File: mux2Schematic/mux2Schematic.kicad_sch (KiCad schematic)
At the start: 1 part

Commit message: Jackson Schematic Work
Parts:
- added H1, H2, H3, H4: MountingHole, symbol Mechanical:MountingHole
- added J1: Conn_02x12_Odd_Even, symbol Connector_Generic:Conn_02x12_Odd_Even
- added J2: Conn_02x06_Top_Bottom, symbol Connector_Generic:Conn_02x06_Top_Bottom
- added J3, J4: ~, symbol HRL_Custom:Banana_Connector_THT
- added J5, J7: Conn_01x08, symbol Connector_Generic:Conn_01x08
- added J6: ~, symbol HRL_Custom:THT_Wire
- added TP1, TP2, TP3, TP4, TP5, TP6: TestPoint, symbol Connector:TestPoint
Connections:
- net CS_0: now also J2.1 (Pin_1)
- net GND: now also J1.11 (Pin_11), J1.14 (Pin_14), J1.17 (Pin_17), J1.2 (Pin_2), J1.20 (Pin_20), J1.23 (Pin_23), J1.5 (Pin_5), J1.8 (Pin_8), J2.11 (Pin_11), J2.5 (Pin_5); no longer U1.10 (S1), U1.6 (E), U1.7 (V_EE), U1.8 (GND), U1.9 (S2)
- net CS_4: now reaches U1.1 (A4)
- net CS_3: now reaches U1.12 (A3)
- net CS_2: now reaches U1.15 (A2)
- net CS_6: now reaches U1.2 (A6)
- net CS_7: now reaches U1.4 (A7)
- net CS_5: now reaches U1.5 (A5)
- new net: U1.6 (E), U1.7 (V_EE), U1.8 (GND)
- new net CIPO: J2.3 (Pin_3)
- new net COPI: J2.2 (Pin_2)
- new net IOVcc: J2.12 (Pin_12), J2.6 (Pin_6)
- new net OGND: TP3.1, TP5.1
- new net S1: U1.10 (S1)
- new net S2: U1.9 (S2)
- new net SCLK: J2.4 (Pin_4)
- new net Vout_0: J5.1 (Pin_1), TP2.1
- new net Vout_1: J5.2 (Pin_2), TP4.1
- new net supplyGND: J4.
- new net supplyPower: J3.
- new net ~{CLR}: J2.9 (Pin_9)
- new net ~{LDAC}: J2.7 (Pin_7)
- new net ~{RESET}: J2.8 (Pin_8)
- no-connect marks 6 -> 1
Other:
- note added: "8x output SMA blocks"
- note added: "Bot Row"
- note added: "Cap ?"
- note added: "Connectors to VCC on side"
- note added: "LDO 1 to IOVcc supply to 1V8 *Certain*"
- note added: "LDO 2 to VCC supply to 3V3 *Pretty Certain*"
- note added: "October 30, 2024"
- note added: "PCBv1.1 HRL Labs Harvey Mudd Clinic Team"
- note added: "Relevant Testpoints"
- note added: "SMA?"
- note added: "Through Hole or Surface Mount?"
- note added: "Top Row"
- note added: "or"
- moved on the sheet: U1

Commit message: Schematic Draft 1
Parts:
- removed J7: Conn_01x08, symbol Connector_Generic:Conn_01x08
- removed TP1, TP6: TestPoint, symbol Connector:TestPoint
- added C1: 0.1µF, symbol Device:C
- added J10, J11, J12, J13, J14, J7, J9: Conn_02x06_Top_Bottom, symbol Connector_Generic:Conn_02x06_Top_Bottom
- added J15, J16, J17, J18, J19, J20, J21: ~, symbol HRL_Custom:THT_Wire
- added J8: Conn_01x10, symbol Connector_Generic:Conn_01x10
- added JP1: SolderJumper_2_Bridged, symbol Jumper:SolderJumper_2_Bridged
- added JP2: SolderJumper_2_Open, symbol Jumper:SolderJumper_2_Open
- added TP10, TP11, TP12, TP13, TP14, TP15, TP16, TP17, TP18, TP7, TP8, TP9: TestPoint, symbol Connector:TestPoint
- added U2: AMS1117-1.8, Package_TO_SOT_SMD:SOT-223-3_TabPin2, symbol Regulator_Linear:AMS1117-1.8
- added U3: AZ1084-3.3, symbol Regulator_Linear:AZ1084-3.3
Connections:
- net supplyGND is gone; now on net GND: J4.
- net CIPO: now also J10.3 (Pin_3), J11.3 (Pin_3), J12.3 (Pin_3), J13.3 (Pin_3), J14.3 (Pin_3), J7.3 (Pin_3), J9.3 (Pin_3)
- net COPI: now also J10.2 (Pin_2), J11.2 (Pin_2), J12.2 (Pin_2), J13.2 (Pin_2), J14.2 (Pin_2), J7.2 (Pin_2), J8.5 (Pin_5), J9.2 (Pin_2)
- net CS: now also J8.6 (Pin_6)
- net CS_1: now also J7.1 (Pin_1)
- net CS_2: now also J9.1 (Pin_1)
- net CS_3: now also J10.1 (Pin_1)
- net CS_4: now also J11.1 (Pin_1)
- net CS_5: now also J13.1 (Pin_1)
- net CS_6: now also J12.1 (Pin_1)
- net CS_7: now also J14.1 (Pin_1)
- net GND: now also U1.6 (E), U1.7 (V_EE), U1.8 (GND), C1.2, J10.11 (Pin_11), J10.5 (Pin_5), J11.11 (Pin_11), J11.5 (Pin_5), J12.11 (Pin_11), J12.5 (Pin_5), J13.11 (Pin_11), J13.5 (Pin_5), J14.11 (Pin_11), J14.5 (Pin_5), J7.11 (Pin_11), J7.5 (Pin_5), J9.11 (Pin_11), J9.5 (Pin_5), U2.1 (GND), U3.1 (GND)
- net IOVcc: now also J10.12 (Pin_12), J10.6 (Pin_6), J11.12 (Pin_12), J11.6 (Pin_6), J12.12 (Pin_12), J12.6 (Pin_6), J13.12 (Pin_12), J13.6 (Pin_6), J14.12 (Pin_12), J14.6 (Pin_6), J7.12 (Pin_12), J7.6 (Pin_6), J9.12 (Pin_12), J9.6 (Pin_6), U2.2 (VO)
- net OGND: now also TP4.1, TP11.1, TP13.1, TP15.1, TP17.1, TP7.1, TP9.1; no longer TP5.1
- net S0: now also J8.1 (Pin_1)
- net S1: now also J8.2 (Pin_2)
- net S2: now also J8.3 (Pin_3)
- net SCLK: now also J10.4 (Pin_4), J11.4 (Pin_4), J12.4 (Pin_4), J13.4 (Pin_4), J14.4 (Pin_4), J7.4 (Pin_4), J8.4 (Pin_4), J9.4 (Pin_4)
- net VCC: now also J6., J15., J16., J17., J18., J19., J20., J21., JP1.2 (B), U3.2 (VO)
- net Vout_1: now also TP5.1; no longer TP4.1
- net muxPower: now also U1.16 (VCC), C1.1, JP1.1 (A), JP2.2 (B)
- net supplyPower: now also JP2.1 (A), U2.3 (VI), U3.3 (VI)
- net ~{CLR}: now also J10.9 (Pin_9), J11.9 (Pin_9), J12.9 (Pin_9), J13.9 (Pin_9), J14.9 (Pin_9), J7.9 (Pin_9), J8.9 (Pin_9), J9.9 (Pin_9)
- net ~{LDAC}: now also J10.7 (Pin_7), J11.7 (Pin_7), J12.7 (Pin_7), J13.7 (Pin_7), J14.7 (Pin_7), J7.7 (Pin_7), J8.7 (Pin_7), J9.7 (Pin_7)
- net ~{RESET}: now also J10.8 (Pin_8), J11.8 (Pin_8), J12.8 (Pin_8), J13.8 (Pin_8), J14.8 (Pin_8), J7.8 (Pin_8), J8.8 (Pin_8), J9.8 (Pin_8)
- net Vout_2: now reaches J5.3 (Pin_3)
- net Vout_2: now also TP8.1
- net Vout_3: now reaches J5.4 (Pin_4)
- net Vout_3: now also TP10.1
- net Vout_4: now reaches J5.5 (Pin_5)
- net Vout_4: now also TP12.1
- net Vout_5: now reaches J5.6 (Pin_6)
- net Vout_5: now also TP14.1
- net Vout_6: now reaches J5.7 (Pin_7)
- net Vout_6: now also TP16.1
- net Vout_7: now reaches J5.8 (Pin_8)
- net Vout_7: now also TP18.1
- no-connect marks 1 -> 9
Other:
- note added: "8x DAC output blocks"
- note added: "Additional Testpoints"
- note added: "Mux Power and Logic"
- note added: "Power"
- note added: "VCC Ports for Side"
- note added: "Xilinx Digital Input"
- note removed: "8x output SMA blocks"
- note removed: "Cap ?"
- note removed: "Connectors to VCC on side"
- note removed: "LDO 1 to IOVcc supply to 1V8 *Certain*"
- note removed: "LDO 2 to VCC supply to 3V3 *Pretty Certain*"
- note removed: "Relevant Testpoints"
- note removed: "Through Hole or Surface Mount?"
- note removed: "or"
- moved on the sheet: H1, H2, H3, H4, J1, J2, J3, J4, J5, J6, TP2, TP3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

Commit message: Final Draft Schematic
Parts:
- removed J5: Conn_01x08, symbol Connector_Generic:Conn_01x08
- added C2, C4: 10uF, symbol Device:C_Polarized
- added C3, C5: 22uF, symbol Device:C_Polarized
- added J22, J23, J24, J25, J26, J27, J28, J29: ~, symbol HRL_Custom:SMA_Connector
- added J30, J31, J5: Conn_01x10, symbol Connector_Generic:Conn_01x10
- added R1, R2, R3, R4, R5, R6, R7, R8: 10k, symbol Device:R
- C1: value 0.1µF -> 0.1uF
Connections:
- net CS_0: now also J30.1 (Pin_1), R1.1
- net CS_1: now also J30.2 (Pin_2), R2.1
- net CS_2: now also J30.3 (Pin_3), R3.1
- net CS_3: now also J30.4 (Pin_4), R4.1
- net CS_4: now also J30.5 (Pin_5), R5.1
- net CS_5: now also J30.6 (Pin_6), R6.1
- net CS_6: now also J30.7 (Pin_7), R7.1
- net CS_7: now also J30.8 (Pin_8), R8.1
- net GND: now also J8.10 (Pin_10), C2.2, C3.2, C4.2, C5.2, J30.10 (Pin_10), J30.9 (Pin_9)
- net IOVcc: now also C5.1, R1.2, R2.2, R3.2, R4.2, R5.2, R6.2, R7.2, R8.2
- net VCC: now also C3.1
- net Vout_0: now also J22.Center, J31.1 (Pin_1)
- net Vout_1: now also J23.Center, J31.2 (Pin_2)
- net Vout_2: now also J24.Center, J31.3 (Pin_3)
- net Vout_3: now also J25.Center, J31.4 (Pin_4)
- net Vout_4: now also J26.Center, J31.5 (Pin_5)
- net Vout_5: now also J27.Center, J31.6 (Pin_6)
- net Vout_6: now also J28.Center, J31.7 (Pin_7)
- net Vout_7: now also J29.Center, J31.8 (Pin_8)
- net supplyPower: now also C2.1, C4.1
- removed net OGND: TP11.1, TP13.1, TP15.1, TP17.1, TP3.1, TP4.1, TP7.1, TP9.1
- new net OGND_0: J22.Shield, J5.1 (Pin_1), TP3.1
- new net OGND_1: J23.Shield, J5.2 (Pin_2), TP4.1
- new net OGND_2: J24.Shield, J5.3 (Pin_3), TP7.1
- new net OGND_3: J25.Shield, J5.4 (Pin_4), TP9.1
- new net OGND_4: J26.Shield, J5.5 (Pin_5), TP11.1
- new net OGND_5: J27.Shield, J5.6 (Pin_6), TP13.1
- new net OGND_6: J28.Shield, J5.7 (Pin_7), TP15.1
- new net OGND_7: J29.Shield, J5.8 (Pin_8), TP17.1
- no-connect marks 9 -> 12
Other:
- note added: "CS_x Pull Up Resistors"
- note removed: "SMA?"
- moved on the sheet: C1, J15, J16, J17, J18, J19, J20, J21, J6, JP1, JP2, TP11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

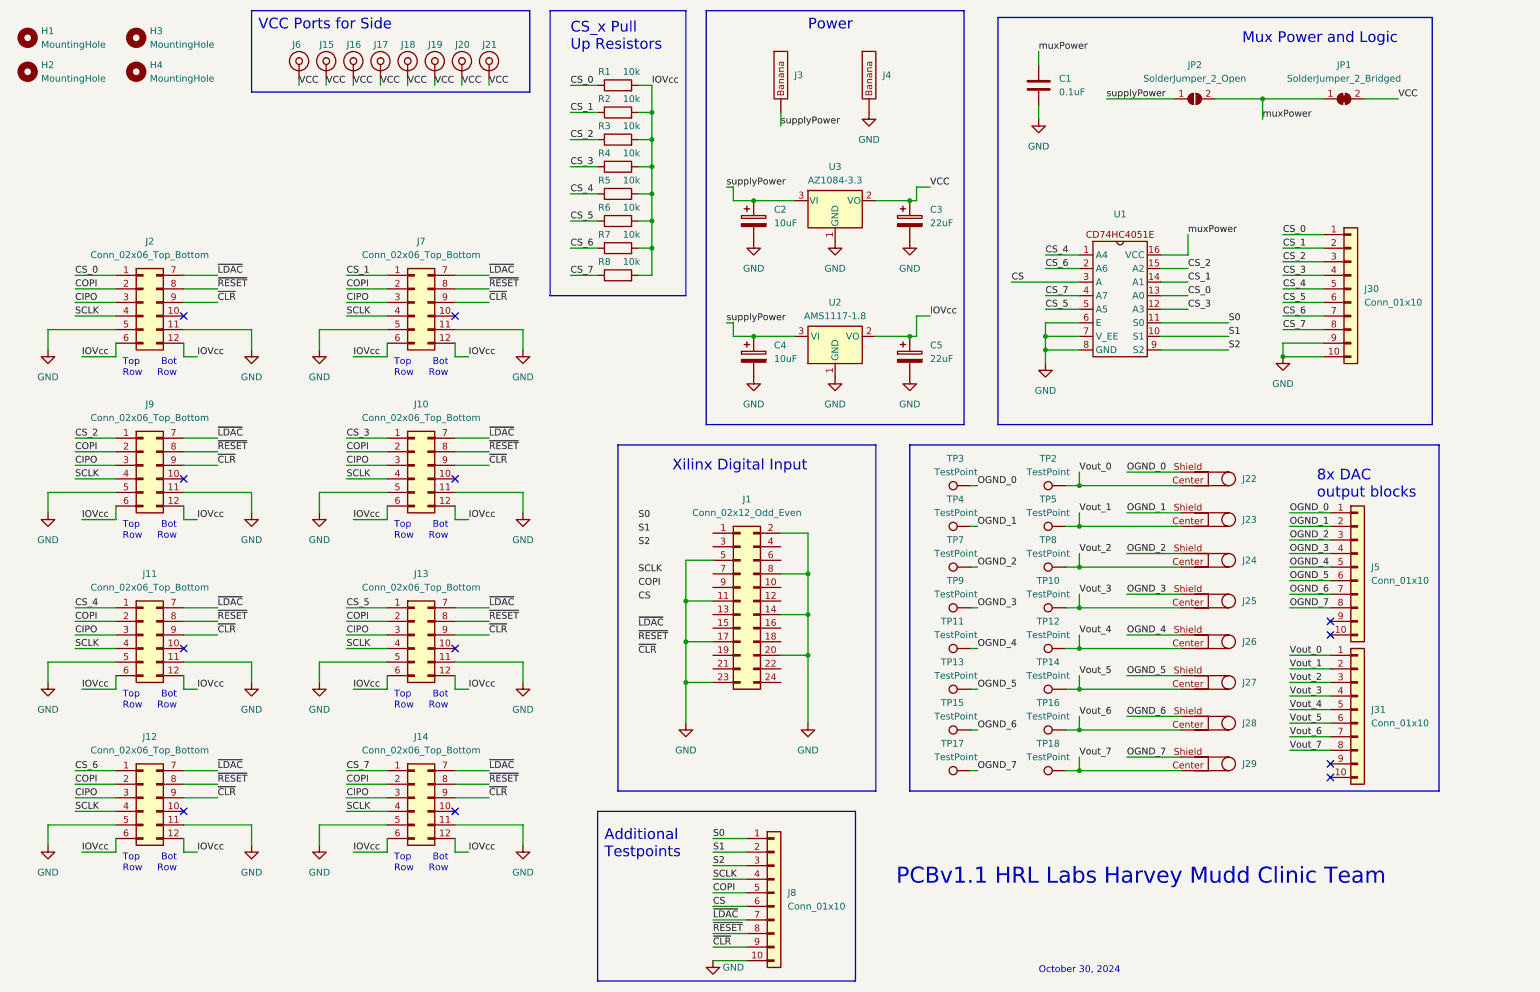
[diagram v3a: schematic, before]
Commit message: Update 1x2 Headers on Vcc
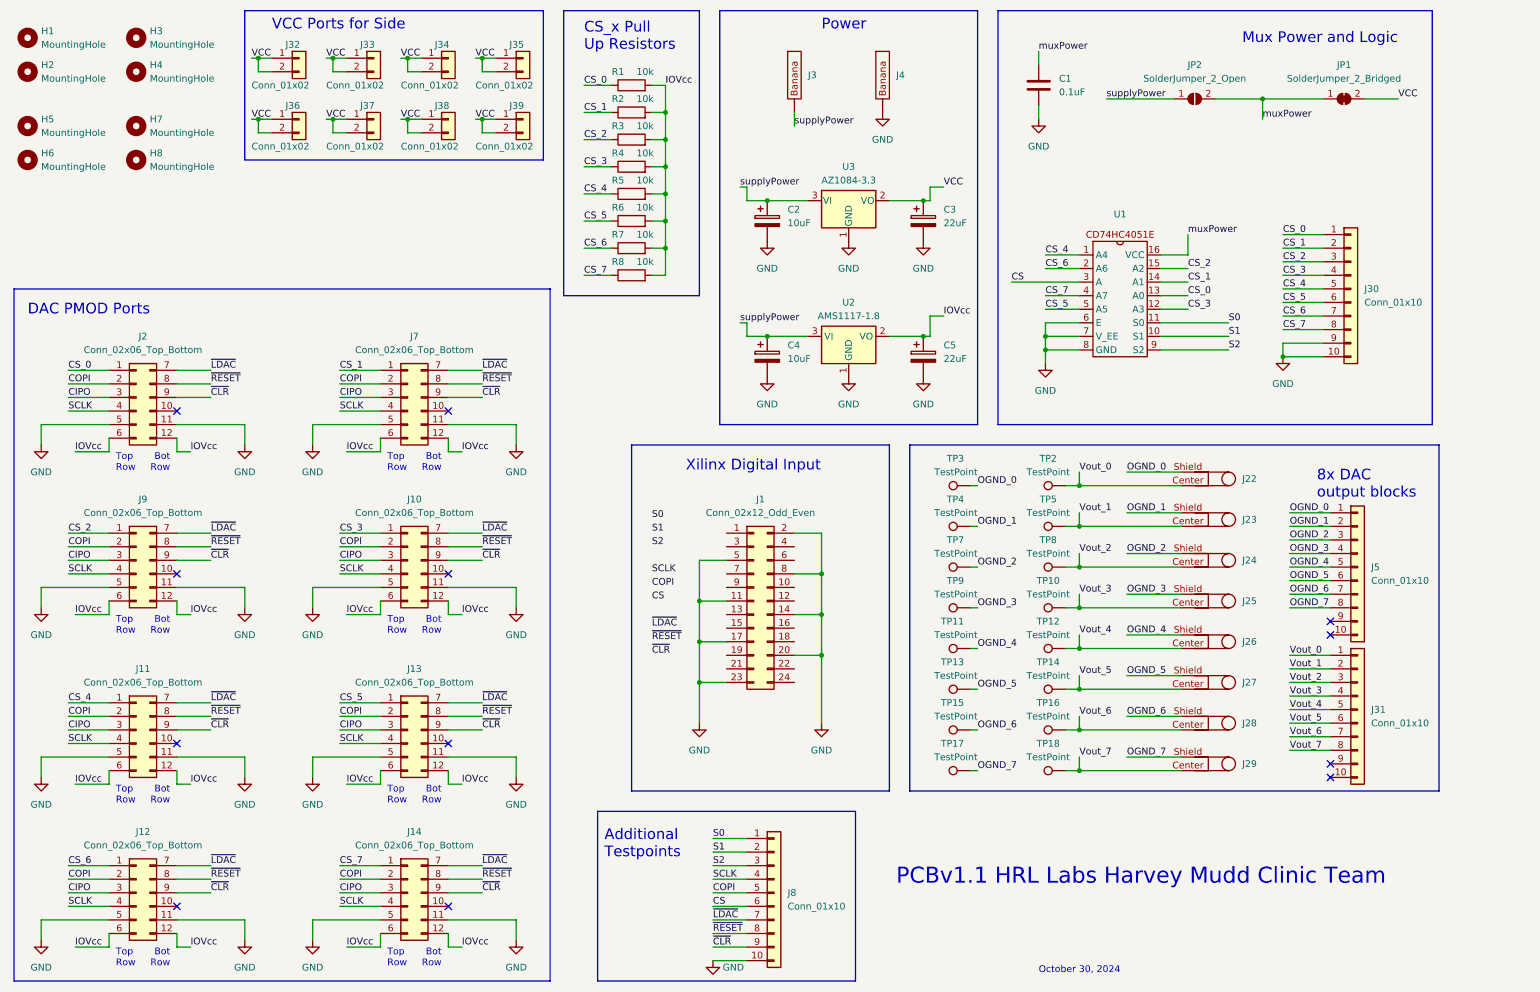
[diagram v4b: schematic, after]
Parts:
- removed J15, J16, J17, J18, J19, J20, J21, J6: ~, symbol HRL_Custom:THT_Wire
- added H5, H6, H7, H8: MountingHole, symbol Mechanical:MountingHole
- added J32, J33, J34, J35, J36, J37, J38, J39: Conn_01x02, symbol Connector_Generic:Conn_01x02
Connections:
- net VCC: now also J32.1 (Pin_1), J32.2 (Pin_2), J33.1 (Pin_1), J33.2 (Pin_2), J34.1 (Pin_1), J34.2 (Pin_2), J35.1 (Pin_1), J35.2 (Pin_2), J36.1 (Pin_1), J36.2 (Pin_2), J37.1 (Pin_1), J37.2 (Pin_2), J38.1 (Pin_1), J38.2 (Pin_2), J39.1 (Pin_1), J39.2 (Pin_2)
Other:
- note added: "DAC PMOD Ports"
- moved on the sheet: C2, C3, C4, C5, J1, J10, J11, J12, J13, J14, J2, J3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

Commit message: First Draft of PCB
Haven't routed traces in case of major feedback from Prof. Brake tomorrow
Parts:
- removed JP1: SolderJumper_2_Bridged, symbol Jumper:SolderJumper_2_Bridged
- removed JP2: SolderJumper_2_Open, symbol Jumper:SolderJumper_2_Open
- removed TP10, TP11, TP12, TP13, TP14, TP15, TP16, TP17, TP18, TP2, TP3, TP4, TP5, TP7, TP8, TP9: TestPoint, symbol Connector:TestPoint
- added J15, J16, J17, J18, J19, J20, J21, J6: Conn_01x02, Connector_PinSocket_2.54mm:PinSocket_1x02_P2.54mm_Vertical, symbol Connector_Generic:Conn_01x02
- added JP3: SolderJumper_3_Bridged12, Jumper:SolderJumper-3_P1.3mm_Bridged12_RoundedPad1.0x1.5mm, symbol Jumper:SolderJumper_3_Bridged12
- C1, C2, C3, C4, C5: footprint (none) -> Capacitor_SMD:C_0805_2012Metric
- H1, H2, H3, H4, H5, H6, H7, H8: footprint (none) -> MountingHole:MountingHole_3.2mm_M3
- J1: footprint (none) -> Connector_IDC:IDC-Header_2x12_P2.54mm_Vertical
- J10, J11, J12, J13, J14, J2, J7, J9: footprint (none) -> Connector_PinSocket_2.54mm:PinSocket_2x06_P2.54mm_Horizontal
- J22, J23, J24, J25, J26, J27, J28, J29: footprint (none) -> Connector_Coaxial:SMA_Amphenol_132134-16_Vertical
- J3, J4: value ~ -> Banana; footprint (none) -> MountingHole:MountingHole_6.4mm_M6_DIN965_Pad
- J30, J31, J5: value Conn_01x10 -> Conn_01x8; footprint (none) -> Connector_PinHeader_2.54mm:PinHeader_1x08_P2.54mm_Vertical; symbol Connector_Generic:Conn_01x10 -> Connector_Generic:Conn_01x08
- J32, J33, J34, J35, J36, J37, J38, J39: footprint (none) -> Connector_PinSocket_2.54mm:PinSocket_1x02_P2.54mm_Vertical
- J8: footprint (none) -> Connector_PinHeader_2.54mm:PinHeader_1x10_P2.54mm_Vertical
- R1, R2, R3, R4, R5, R6, R7, R8: footprint (none) -> Resistor_SMD:R_0805_2012Metric
- U1: value ~ -> CD74HC4051E; footprint (none) -> Package_SO:TSSOP-16_4.4x5mm_P0.65mm
- U3: footprint (none) -> Package_TO_SOT_SMD:TO-252-3_TabPin2
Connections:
- net GND: now also J4.1; no longer J30.10 (Pin_10), J30.9 (Pin_9), J4.
- net OGND_0: now also J22.2, J5.2 (Pin_2), J6.2 (Pin_2); no longer J22.Shield, J5.1 (Pin_1)
- net OGND_1: now also J23.2, J5.4 (Pin_4), J15.2 (Pin_2); no longer J23.Shield, J5.2 (Pin_2)
- net OGND_2: now also J24.2, J5.6 (Pin_6), J16.2 (Pin_2); no longer J24.Shield, J5.3 (Pin_3)
- net OGND_3: now also J25.2, J5.8 (Pin_8), J17.2 (Pin_2); no longer J25.Shield, J5.4 (Pin_4)
- net OGND_4: now also J26.2, J31.2 (Pin_2), J18.2 (Pin_2); no longer J26.Shield, J5.5 (Pin_5)
- net OGND_5: now also J27.2, J31.4 (Pin_4), J19.2 (Pin_2); no longer J27.Shield, J5.6 (Pin_6)
- net OGND_6: now also J28.2, J31.6 (Pin_6), J20.2 (Pin_2); no longer J28.Shield, J5.7 (Pin_7)
- net OGND_7: now also J29.2, J31.8 (Pin_8), J21.2 (Pin_2); no longer J29.Shield, J5.8 (Pin_8)
- net VCC: now also JP3.1 (A)
- net Vout_0: now also J22.1, J5.1 (Pin_1), J6.1 (Pin_1); no longer J22.Center, J31.1 (Pin_1)
- net Vout_1: now also J23.1, J5.3 (Pin_3), J15.1 (Pin_1); no longer J23.Center, J31.2 (Pin_2)
- net Vout_2: now also J24.1, J5.5 (Pin_5), J16.1 (Pin_1); no longer J24.Center, J31.3 (Pin_3)
- net Vout_3: now also J25.1, J5.7 (Pin_7), J17.1 (Pin_1); no longer J25.Center, J31.4 (Pin_4)
- net Vout_4: now also J26.1, J31.1 (Pin_1), J18.1 (Pin_1); no longer J26.Center, J31.5 (Pin_5)
- net Vout_5: now also J27.1, J31.3 (Pin_3), J19.1 (Pin_1); no longer J27.Center, J31.6 (Pin_6)
- net Vout_6: now also J28.1, J31.5 (Pin_5), J20.1 (Pin_1); no longer J28.Center, J31.7 (Pin_7)
- net Vout_7: now also J29.1, J31.7 (Pin_7), J21.1 (Pin_1); no longer J29.Center, J31.8 (Pin_8)
- net muxPower: now also JP3.2 (C)
- net supplyPower: now also J3.1, JP3.3 (B); no longer J3.
- no-connect marks 12 -> 8
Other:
- note added: "8x DAC Output SMA"
- note added: "VCC Ports for Side of DACs"
- note removed: "8x DAC output blocks"
- note removed: "VCC Ports for Side"
- moved on the sheet: C1, J1, J22, J23, J24, J25, J26, J27, J28, J29, J3, J32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

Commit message: minor tweaks to PCB
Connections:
- net CIPO: now also J1.16 (Pin_16)
- net COPI: now also J1.18 (Pin_18)
- net CS: now also J1.19 (Pin_19)
- net S0: now also J1.22 (Pin_22)
- net S1: now also J1.24 (Pin_24)
- net S2: now also J1.21 (Pin_21)
- net SCLK: now also J1.12 (Pin_12)
- net ~{CLR}: now also J1.4 (Pin_4)
- net ~{LDAC}: now also J1.10 (Pin_10)
- net ~{RESET}: now also J1.6 (Pin_6)
- no-connect marks 8 -> 14
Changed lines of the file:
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@@
 	)
 	(no_connect
+		(at 162.56 119.38)
+	)
+	(no_connect
 		(at 96.52 181.61)
 	)
 	(no_connect
+		(at 162.56 121.92)
+	)
+	(no_connect
 		(at 45.72 151.13)
 	)
@@
 	)
 	(no_connect
+		(at 162.56 127)
+	)
+	(no_connect
 		(at 45.72 88.9)
 	)
 	(no_connect
+		(at 162.56 111.76)
+	)
+	(no_connect
 		(at 45.72 181.61)
 	)
 	(no_connect
+		(at 162.56 114.3)
+	)
+	(no_connect
 		(at 96.52 88.9)
 	)
 	(no_connect
+		(at 162.56 129.54)
+	)
+	(no_connect
 		(at 96.52 119.38)
 	)
@@
 	)
 	(label "SCLK"
-		(at 182.88 119.38 0)
+		(at 175.26 124.46 0)
 		(fields_autoplaced yes)
 		(effects
@@
 	)
 	(label "~{RESET}"
-		(at 182.88 132.08 0)
+		(at 175.26 116.84 0)
 		(fields_autoplaced yes)
 		(effects
@@
 	)
 	(label "COPI"
-		(at 182.88 121.92 0)
+		(at 175.26 132.08 0)
 		(fields_autoplaced yes)
 		(effects
@@
 		)
 	)
+	(label "CIPO"
+		(at 175.26 129.54 0)
+		(fields_autoplaced yes)
+		(effects
+			(font
+				(size 1.27 1.27)
+			)
+			(justify left bottom)
+		)
+	)
 	(label "OGND_7"
 		(at 254 152.4 0)
@@
 	)
 	(label "S2"
-		(at 182.88 114.3 0)
+		(at 162.56 137.16 180)
 		(fields_autoplaced yes)
 		(effects
@@
 				(size 1.27 1.27)
 			)
-			(justify left bottom)
+			(justify right bottom)
 		)
 	)
@@
 	)
 	(label "S0"
-		(at 182.88 109.22 0)
+		(at 175.26 137.16 0)
 		(fields_autoplaced yes)
 		(effects
@@
 	)
 	(label "S1"
-		(at 182.88 111.76 0)
+		(at 175.26 139.7 0)
 		(fields_autoplaced yes)
 		(effects
@@
 	)
 	(label "~{LDAC}"
-		(at 182.88 129.54 0)
+		(at 175.26 121.92 0)
 		(fields_autoplaced yes)
 		(effects
@@
 	)
 	(label "~{CLR}"
-		(at 182.88 134.62 0)
+		(at 175.26 114.3 0)
 		(fields_autoplaced yes)
 		(effects
@@
 	)
 	(label "CS"
-		(at 182.88 124.46 0)
+		(at 162.56 134.62 180)
 		(fields_autoplaced yes)
 		(effects
@@
 				(size 1.27 1.27)
 			)
-			(justify left bottom)
+			(justify right bottom)
 		)
 	)
